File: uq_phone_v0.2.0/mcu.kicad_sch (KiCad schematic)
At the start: 40 parts, among them J6 Conn_ARM_SWD_TagConnect_TC2030, J7 559092474, J9 559092474, Q1 MMBT3904LP-7, Q2 MMBT3904LP-7, U17 TXU0204DTRR, U18 TXU0304DTRR, U19 TXU0104DTRR, U20 TXU0104DTRR, U5 TCA9509MRVHR, U6 STM32H733VGHx

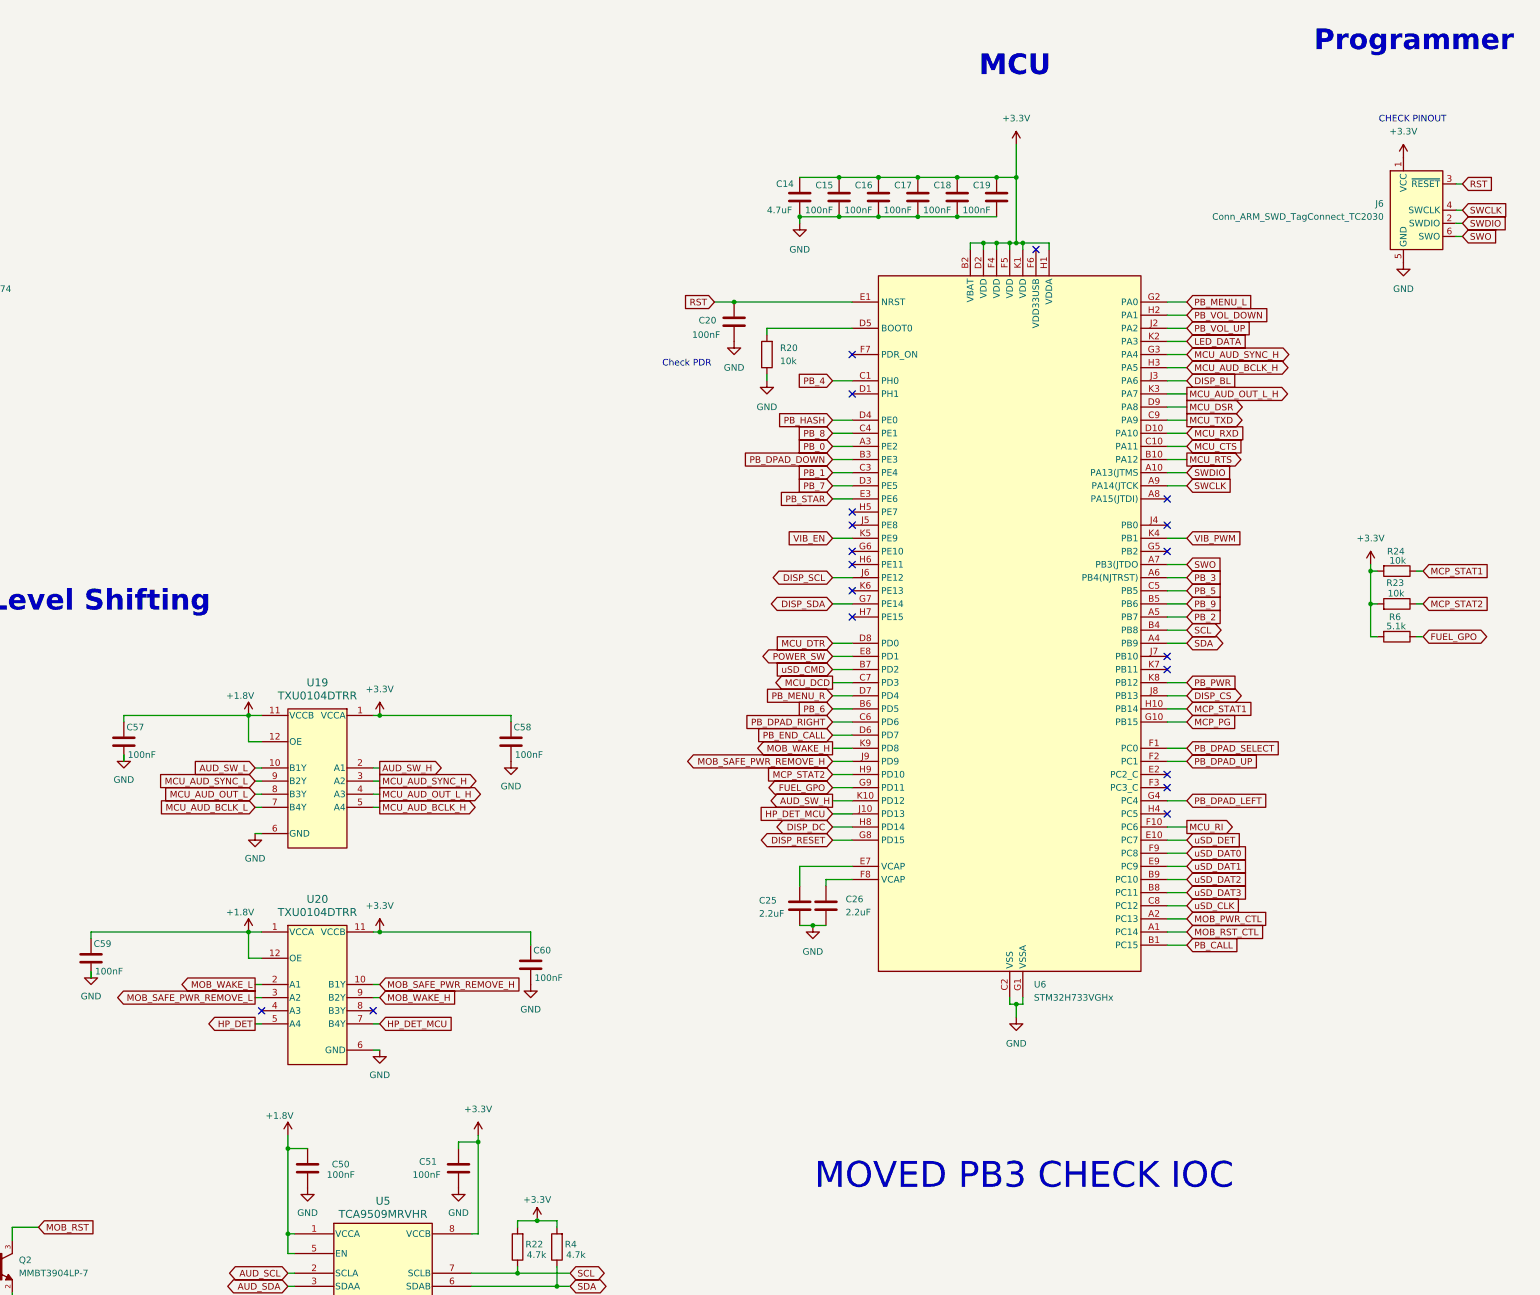
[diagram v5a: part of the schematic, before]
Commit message: Fixed display pinout
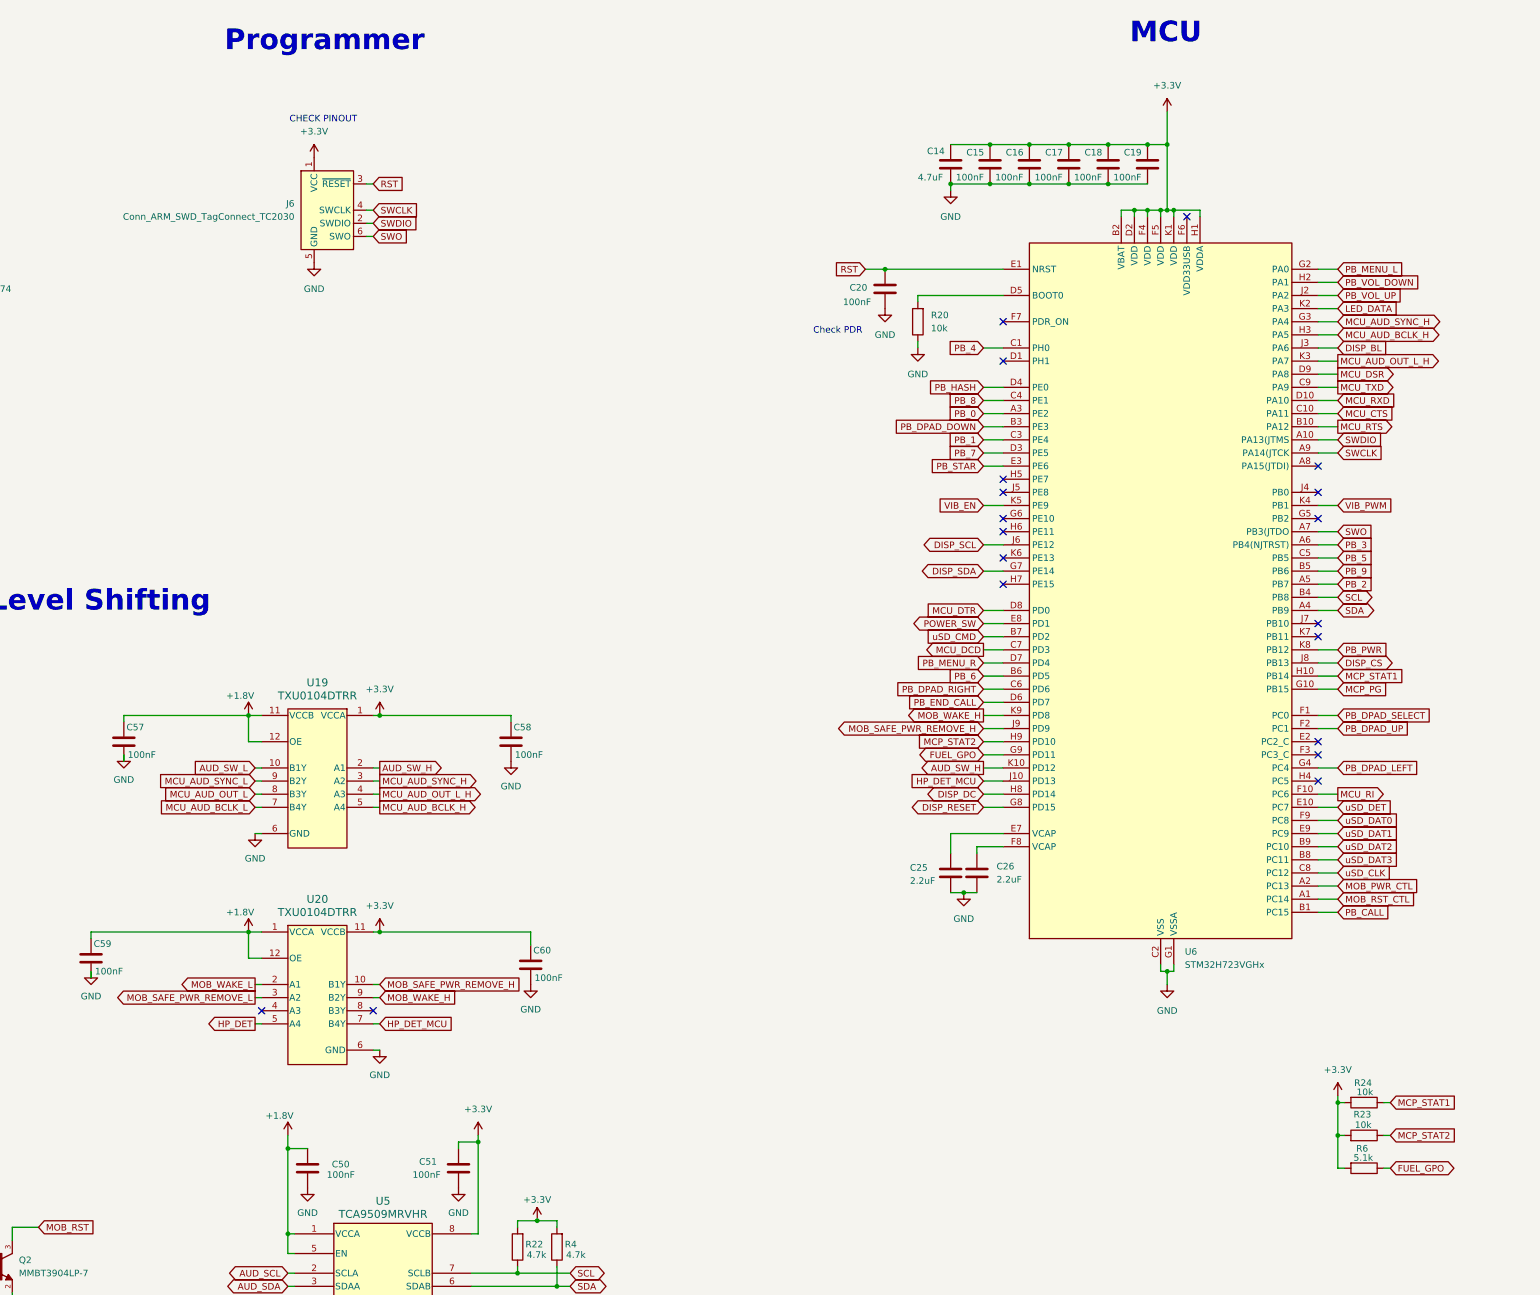
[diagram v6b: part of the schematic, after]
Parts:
- removed U6: STM32H733VGHx, Package_BGA:TFBGA-100_8x8mm_Layout10x10_P0.8mm, symbol MCU_ST_STM32H7:STM32H733VGHx
- added U6: STM32H723VGHx, Package_BGA:TFBGA-100_8x8mm_Layout10x10_P0.8mm, symbol MCU_ST_STM32H7:STM32H723VGHx
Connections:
- net +3.3V: now also U6.B2 (VBAT), U6.D2 (VDD), U6.F4 (VDD), U6.F5 (VDD), U6.H1 (VDDA), U6.K1 (VDD)
- net AUD_SW_H: now also U6.K10 (PD12)
- net DISP_BL: now also U6.J3 (PA6)
- net DISP_CS: now also U6.J8 (PB13)
- net DISP_DC: now also U6.H8 (PD14)
- net DISP_RESET: now also U6.G8 (PD15)
- net DISP_SCL: now also U6.J6 (PE12)
- net DISP_SDA: now also U6.G7 (PE14)
- net FUEL_GPO: now also U6.G9 (PD11)
- net GND: now also U6.C2 (VSS), U6.E4 (VSS), U6.E5 (VSS), U6.E6 (VSS), U6.G1 (VSSA), U6.J1 (VSS)
- net HP_DET_MCU: now also U6.J10 (PD13)
- net LED_DATA: now also U6.K2 (PA3)
- net MCP_PG: now also U6.G10 (PB15)
- net MCP_STAT1: now also U6.H10 (PB14)
- net MCP_STAT2: now also U6.H9 (PD10)
- net MCU_AUD_BCLK_H: now also U6.H3 (PA5)
- net MCU_AUD_OUT_L_H: now also U6.K3 (PA7)
- net MCU_AUD_SYNC_H: now also U6.G3 (PA4)
- net MCU_CTS: now also U6.C10 (PA11)
- net MCU_DCD: now also U6.C7 (PD3)
- net MCU_DSR: now also U6.D9 (PA8)
- net MCU_DTR: now also U6.D8 (PD0)
- net MCU_RI: now also U6.F10 (PC6)
- net MCU_RTS: now also U6.B10 (PA12)
- net MCU_RXD: now also U6.D10 (PA10)
- net MCU_TXD: now also U6.C9 (PA9)
- net MOB_PWR_CTL: now also U6.A2 (PC13)
- net MOB_RST_CTL: now also U6.A1 (PC14)
- net MOB_SAFE_PWR_REMOVE_H: now also U6.J9 (PD9)
- net MOB_WAKE_H: now also U6.K9 (PD8)
- net PB_0: now also U6.A3 (PE2)
- net PB_1: now also U6.C3 (PE4)
- net PB_2: now also U6.A5 (PB7)
- net PB_3: now also U6.A6 (PB4(NJTRST))
- net PB_4: now also U6.C1 (PH0)
- net PB_5: now also U6.C5 (PB5)
- net PB_6: now also U6.B6 (PD5)
- net PB_7: now also U6.D3 (PE5)
- net PB_8: now also U6.C4 (PE1)
- net PB_9: now also U6.B5 (PB6)
- net PB_CALL: now also U6.B1 (PC15)
- net PB_DPAD_DOWN: now also U6.B3 (PE3)
- net PB_DPAD_LEFT: now also U6.G4 (PC4)
- net PB_DPAD_RIGHT: now also U6.C6 (PD6)
- net PB_DPAD_SELECT: now also U6.F1 (PC0)
- net PB_DPAD_UP: now also U6.F2 (PC1)
- net PB_END_CALL: now also U6.D6 (PD7)
- net PB_HASH: now also U6.D4 (PE0)
- net PB_MENU_L: now also U6.G2 (PA0)
- net PB_MENU_R: now also U6.D7 (PD4)
- net PB_PWR: now also U6.K8 (PB12)
- net PB_STAR: now also U6.E3 (PE6)
- net PB_VOL_DOWN: now also U6.H2 (PA1)
- net PB_VOL_UP: now also U6.J2 (PA2)
- net POWER_SW: now also U6.E8 (PD1)
- net RST: now also U6.E1 (NRST)
- net SCL: now also U6.B4 (PB8)
- net SDA: now also U6.A4 (PB9)
- net SWCLK: now also U6.A9 (PA14(JTCK)
- net SWDIO: now also U6.A10 (PA13(JTMS)
- net SWO: now also U6.A7 (PB3(JTDO)
- net VIB_EN: now also U6.K5 (PE9)
- net VIB_PWM: now also U6.K4 (PB1)
- net uSD_CLK: now also U6.C8 (PC12)
- net uSD_CMD: now also U6.B7 (PD2)
- net uSD_DAT0: now also U6.F9 (PC8)
- net uSD_DAT1: now also U6.E9 (PC9)
- net uSD_DAT2: now also U6.B9 (PC10)
- net uSD_DAT3: now also U6.B8 (PC11)
- net uSD_DET: now also U6.E10 (PC7)
- net at C26.1: now also U6.F8 (VCAP)
- net at R20.2: now also U6.D5 (BOOT0)
- net at C25.1: now also U6.E7 (VCAP)
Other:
- note removed: "MOVED PB3 CHECK IOC"
- moved on the sheet: C14, C15, C16, C17, C18, C19, C20, C25, C26, J6, R20, R23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

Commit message: Cleaning up adn fixing massive mistake
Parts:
- added C21: 100nF, Capacitor_SMD:C_0201_0603Metric, symbol Capacitors:capacitor_100nF
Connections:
- net +3.3V: now also U6.F7 (PDR_ON), C21.2
- net GND: now also C21.1
- net MOB_SAFE_PWR_REMOVE_H: now also U20.9 (B2Y); no longer U20.10 (B1Y)
- net MOB_WAKE_H: now also U20.10 (B1Y); no longer U20.9 (B2Y)
- no-connect marks 19 -> 18
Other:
- note added: "UQ Phone"
- note removed: "CHECK PINOUT"
- note removed: "Check PDR"
- note removed: "Logic Level Shifting"
- note removed: "MCU"
- note removed: "Mezzanine Connectors"
- note removed: "Programmer"
- title: UQ Phone -> Control System
- moved on the sheet: C14, C15, C16, C17, C18, C19, C20, C25, C26, C28, C50, C51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
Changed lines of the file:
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@@
 	(paper "A3")
 	(title_block
-		(title "UQ Phone")
+		(title "Control System")
+		(date "2025-09-05")
 		(rev "0.2.0")
 		(company "The University of Queensland")
+		(comment 1 "James Wood")
 	)
